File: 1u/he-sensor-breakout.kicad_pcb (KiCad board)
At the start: 2 copper layers, 19.1 x 17.8 mm, 28 parts, among them J1 Conn_01x01_Pin, J10 Conn_01x01_Pin, J11 Conn_01x01_Pin, J12 Conn_01x01_Pin, J13 Conn_01x01_Pin, J14 Conn_01x01_Pin, J2 Conn_01x01_Pin, J3 Conn_01x01_Pin, J4 Conn_01x01_Pin, J5 Conn_01x01_Pin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

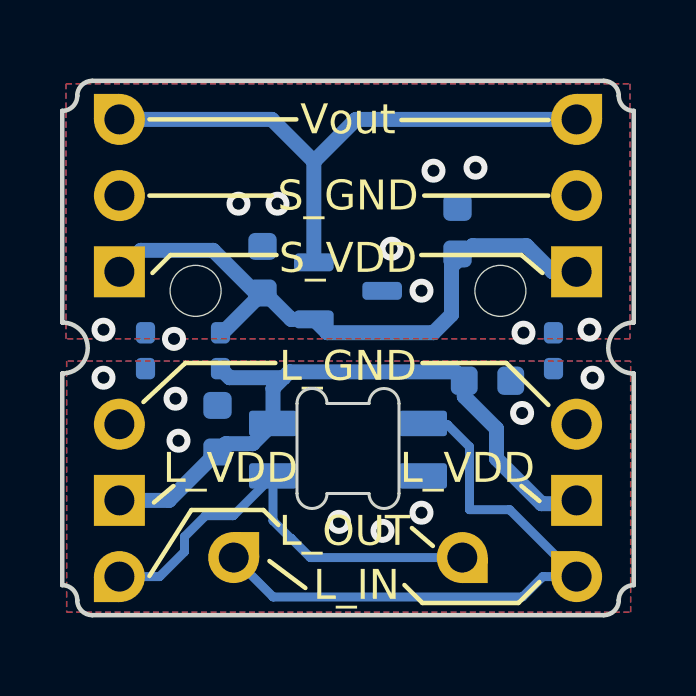
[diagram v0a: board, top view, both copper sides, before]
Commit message: converts to 19.05x19.05mm
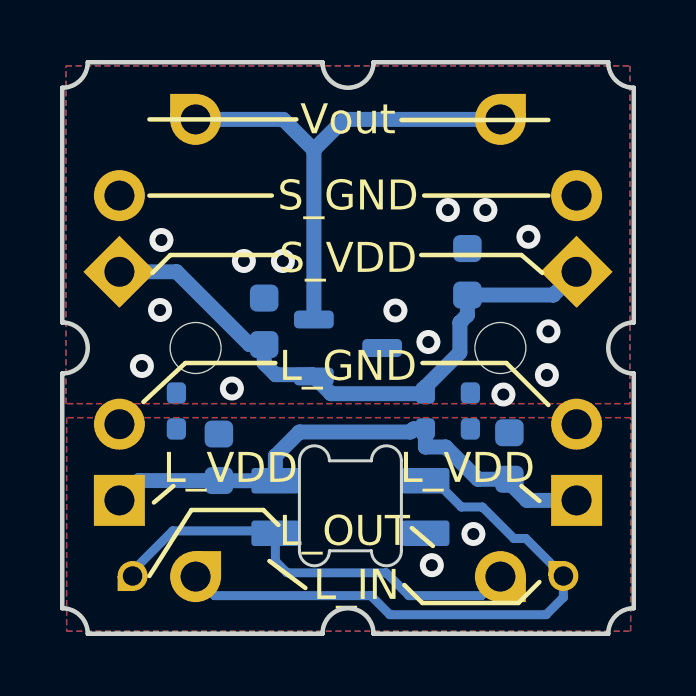
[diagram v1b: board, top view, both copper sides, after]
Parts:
- J11, J13: footprint Connector_PinHeader_2.54mm:PinHeader_1x01_P2.54mm_Vertical -> Connector_PinHeader_1.27mm:PinHeader_1x01_P1.27mm_Vertical
- moved REF** 21.2 mm to (104.5, 91.0), turned to -90 degrees
- moved J12 12.7 mm to (114.3, 109.2), turned to 180 degrees
- moved J14 12.7 mm to (104.1, 109.2), turned to 90 degrees
- moved J13 11.0 mm to (116.4, 109.2)
- moved J11 11.0 mm to (102.0, 109.2), turned to 180 degrees
- moved R3 7.12 mm to (111.8, 103.7)
- moved REF** 4.81 mm to (114.0, 91.0)
- moved R1 3.42 mm to (113.3, 103.7)
- moved C2 2.61 mm to (114.6, 105.2), turned to -90 degrees
- moved J10 2.54 mm to (104.1, 94.0)
- moved J9 2.54 mm to (114.3, 94.0)
- moved R2 2.26 mm to (103.5, 103.7)
- moved D1 1.91 mm to (109.3, 106.9)
- moved SW 1.91 mm to (109.2, 101.6)
- moved U1 1.91 mm to (109.2, 101.6)
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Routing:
- net VDD: track 22.7 -> 17.9 mm
- net Vout: track 19.8 -> 16.7 mm
- net LED_IN: track 20.7 -> 19.7 mm
- net VDDA: track 21.1 -> 20.1 mm
- net GNDD: vias 8 -> 2
- net GNDA: vias 10 -> 14
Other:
- board size 19.1 x 17.8 mm -> 19.1 x 19 mm
